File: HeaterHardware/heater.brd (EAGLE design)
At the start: 70 x 80 mm, 46 parts, among them IC1 MAX31855, IC2 MAX31855, IC3 LM1117IMPX-3.3, IC4 LM1117IMPX-3.3, U1 ATMEGA328P, X1 22-23-2021

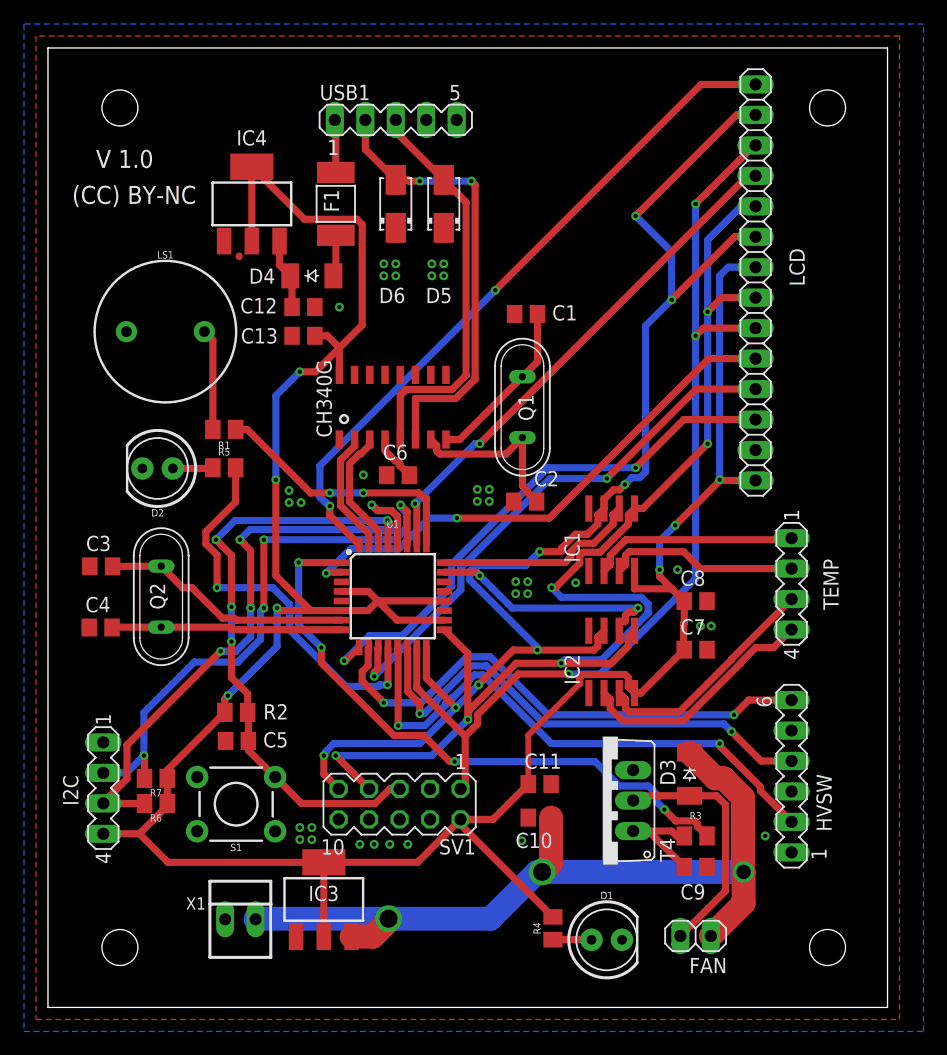
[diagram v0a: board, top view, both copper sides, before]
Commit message: improved routing
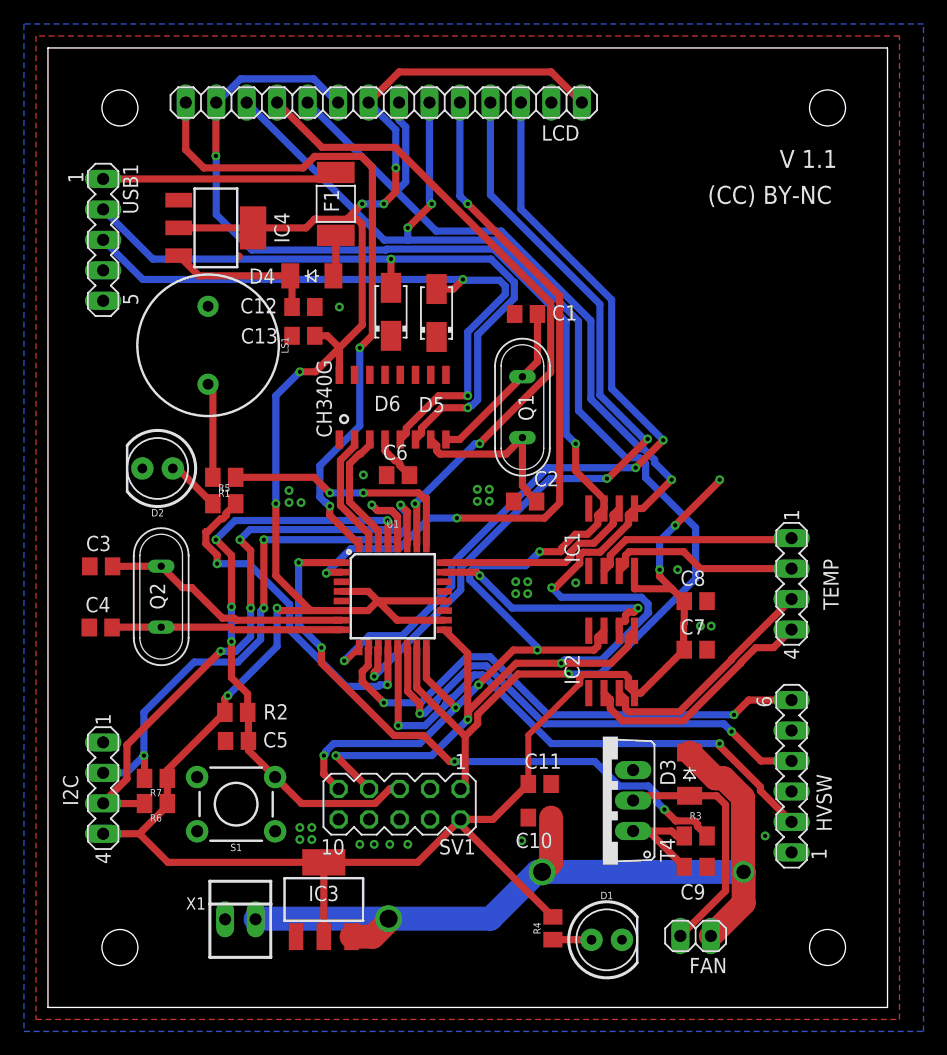
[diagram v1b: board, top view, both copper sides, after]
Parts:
- moved LCD 34.4 mm to (28.0, 75.5), turned to 0 degrees
- moved USB1 26.4 mm to (4.60, 64.0), turned to 270 degrees
- moved D5 9.12 mm to (32.4, 57.9)
- moved D6 9.01 mm to (28.6, 58.0)
- moved R1 4.00 mm to (14.7, 44.2)
- moved LS1 3.74 mm to (13.3, 55.2), turned to 270 degrees
- moved IC4 3.61 mm to (14.0, 65.0), turned to 270 degrees
- moved R5 3.00 mm to (14.7, 42.0)
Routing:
- net MOSI: track 82.2 -> 112.5 mm
- net LCDCS: track 45.4 -> 70.1 mm, vias 2 -> 3
- net SCK: track 106.1 -> 130.5 mm, vias 6 -> 5
- net LCDRST: track 45.3 -> 68.2 mm, vias 2 -> 3
- net D+: track 33.6 -> 55.5 mm, vias 0 -> 2
- net MISO: track 111.7 -> 131.4 mm, vias 8 -> 7
- net D-: track 38.1 -> 57.1 mm
- net LCDDC: track 44.5 -> 60.0 mm, vias 2 -> 3
- net PRE5V: track 4.41 -> 19.6 mm
- net TCS: track 43.2 -> 54.9 mm
- net 3.3V: track 230.6 -> 239.1 mm, vias 7 -> 10
- net N$6: track 5.93 -> 12.7 mm
- net DEBUG: track 33.4 -> 29.5 mm
- net TIRQ: track 57.5 -> 55.6 mm
- net BUZ: track 22.1 -> 20.5 mm
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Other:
- board text added: "V 1.1"
- board text removed: "V 1.0"
